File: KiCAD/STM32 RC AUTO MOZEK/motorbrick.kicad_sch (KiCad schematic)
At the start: 6 parts, among them J2 Conn_01x02_Socket, J3 Conn_01x02_Socket, J4 Conn_01x02_Socket, J5 Conn_01x02_Socket, J6 Conn_01x02_Socket, J7 Conn_01x02_Socket

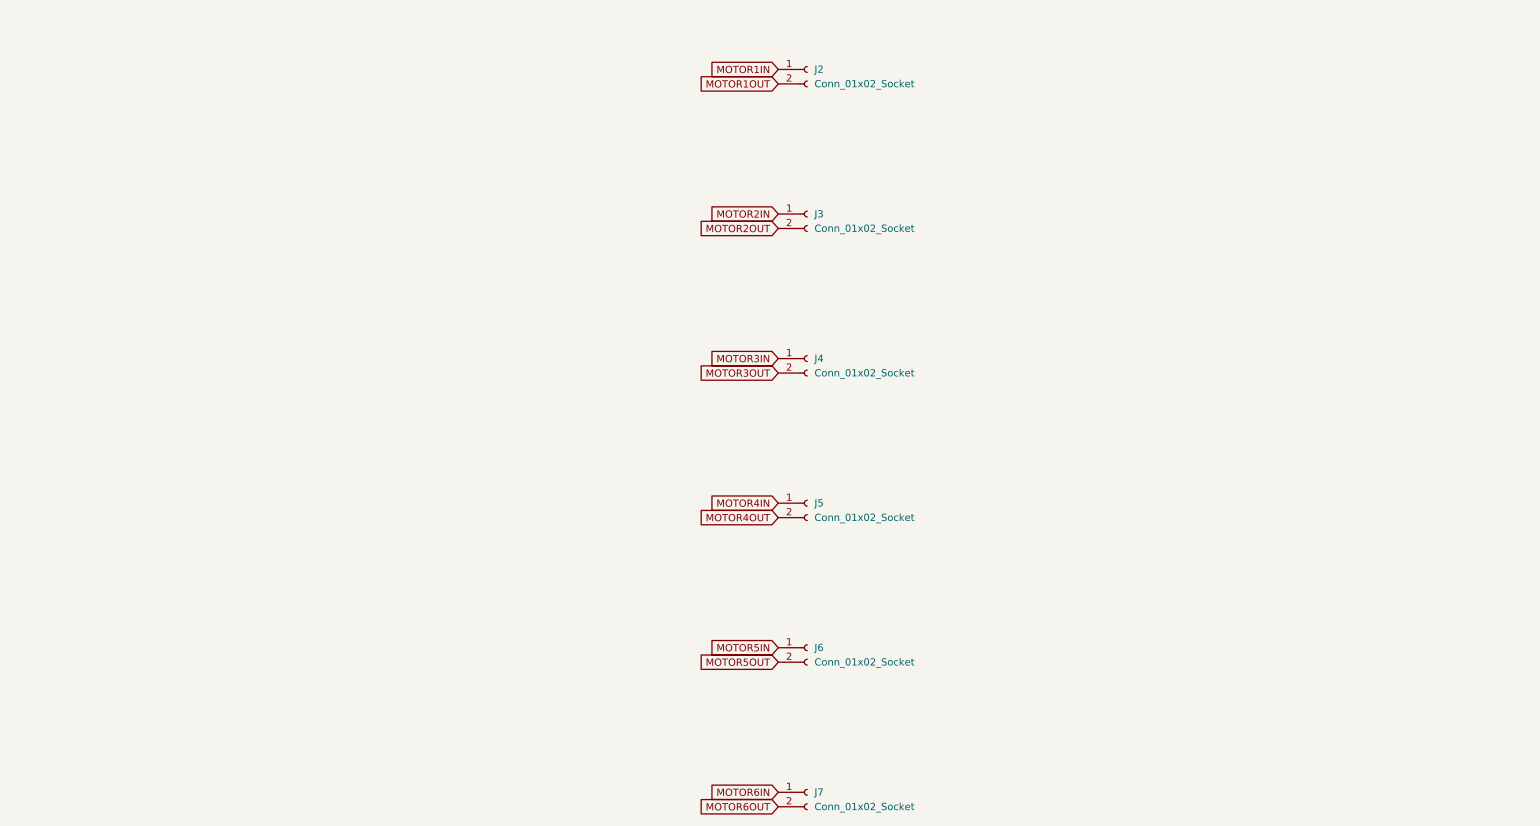
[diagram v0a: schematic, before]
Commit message: Motor power brick implementation
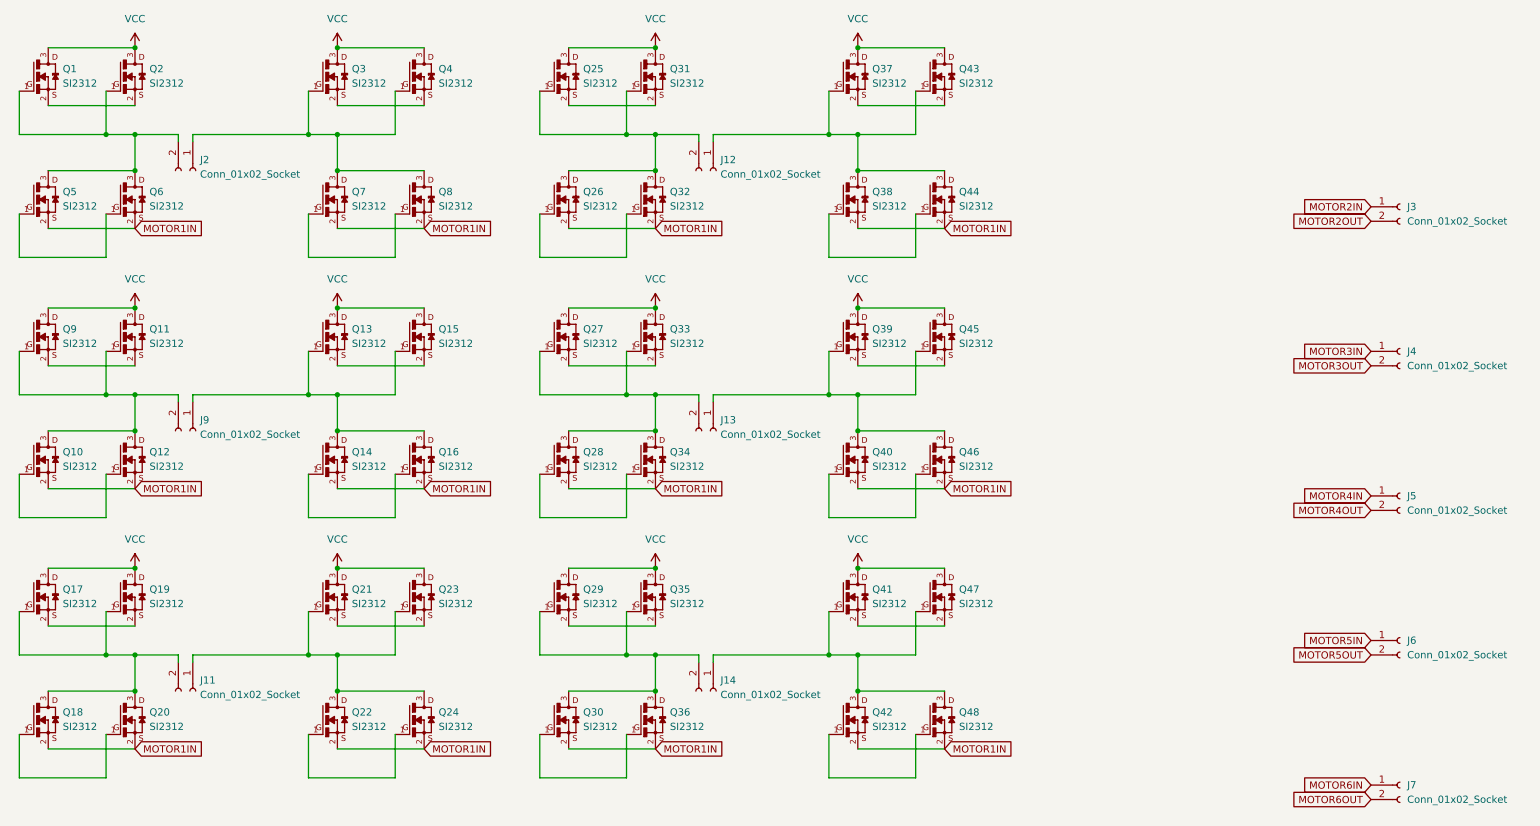
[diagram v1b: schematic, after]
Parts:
- added J11, J12, J13, J14, J9: Conn_01x02_Socket, Connector_Wire:SolderWire-2sqmm_1x02_P7.8mm_D2mm_OD3.9mm_Relief, symbol Connector:Conn_01x02_Socket
- added Q1, Q10, Q11, Q12, Q13, Q14, Q15, Q16, Q17, Q18, Q19, Q2, Q20, Q21, Q22, Q23, Q24, Q25, Q26, Q27, Q28, Q29, Q3, Q30, Q31, Q32, Q33, Q34, Q35, Q36, Q37, Q38, Q39, Q4, Q40, Q41, Q42, Q43, Q44, Q45, Q46, Q47, Q48, Q5, Q6, Q7, Q8, Q9: SI2312, SI2312:SOT23, symbol SI2312:SI2312
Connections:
- net MOTOR1IN: now also Q10.2, Q12.2, Q14.2, Q16.2, Q18.2, Q20.2, Q22.2, Q24.2, Q26.2, Q28.2, Q30.2, Q32.2, Q34.2, Q36.2, Q38.2, Q40.2, Q42.2, Q44.2, Q46.2, Q48.2, Q5.2, Q6.2, Q7.2, Q8.2; no longer J2.1 (Pin_1)
- net MOTOR1OUT: no longer names the net of J2.2 (Pin_2)
- net MOTOR1OUT: now also Q1.1, Q2.1, Q5.3, Q6.3
- new net: Q10.1, Q12.1
- new net: J9.2 (Pin_2), Q10.3, Q11.1, Q12.3, Q9.1
- new net: J11.1 (Pin_1), Q21.1, Q22.3, Q23.1, Q24.3
- new net: Q21.2, Q23.2
- new net: Q11.2, Q9.2
- new net: Q22.1, Q24.1
- new net: Q5.1, Q6.1
- new net: J2.1 (Pin_1), Q3.1, Q4.1, Q7.3, Q8.3
- new net: Q3.2, Q4.2
- new net: Q14.1, Q16.1
- new net: J9.1 (Pin_1), Q13.1, Q14.3, Q15.1, Q16.3
- new net: Q40.1, Q46.1
- new net: J13.1 (Pin_1), Q39.1, Q40.3, Q45.1, Q46.3
- new net: Q42.1, Q48.1
- new net: J14.1 (Pin_1), Q41.1, Q42.3, Q47.1, Q48.3
- new net: Q1.2, Q2.2
- new net: Q18.1, Q20.1
- new net: J11.2 (Pin_2), Q17.1, Q18.3, Q19.1, Q20.3
- new net: J12.1 (Pin_1), Q37.1, Q38.3, Q43.1, Q44.3
- new net: Q37.2, Q43.2
- new net: Q30.1, Q36.1
- new net: J14.2 (Pin_2), Q29.1, Q30.3, Q35.1, Q36.3
- new net: Q39.2, Q45.2
- new net: Q38.1, Q44.1
- new net: Q17.2, Q19.2
- new net: J13.2 (Pin_2), Q27.1, Q28.3, Q33.1, Q34.3
- new net: Q27.2, Q33.2
- new net: Q29.2, Q35.2
- new net: Q28.1, Q34.1
- new net: Q13.2, Q15.2
- new net: Q41.2, Q47.2
- new net: J12.2 (Pin_2), Q25.1, Q26.3, Q31.1, Q32.3
- new net: Q25.2, Q31.2
- new net: Q26.1, Q32.1
- new net: Q7.1, Q8.1
- new net VCC: Q1.3, Q11.3, Q13.3, Q15.3, Q17.3, Q19.3, Q2.3, Q21.3, Q23.3, Q25.3, Q27.3, Q29.3, Q3.3, Q31.3, Q33.3, Q35.3, Q37.3, Q39.3, Q4.3, Q41.3, Q43.3, Q45.3, Q47.3, Q9.3
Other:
- moved on the sheet: J2, J3, J4, J5, J6, J7

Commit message: Multi ADD
Completed work version of code and did more work on schematic
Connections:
- net MOTOR1IN: no longer Q10.2, Q12.2, Q14.2, Q16.2, Q18.2, Q20.2, Q22.2, Q24.2, Q26.2, Q28.2, Q30.2, Q32.2, Q34.2, Q36.2, Q38.2, Q40.2, Q42.2, Q44.2, Q46.2, Q48.2
- net MOTOR2IN: now also Q10.2, Q12.2, Q14.2, Q16.2
- net MOTOR3IN: now also Q18.2, Q20.2, Q22.2, Q24.2
- net MOTOR4IN: now also Q26.2, Q32.2, Q38.2, Q44.2
- net MOTOR5IN: now also Q28.2, Q34.2, Q40.2, Q46.2
- net MOTOR6IN: now also Q30.2, Q36.2, Q42.2, Q48.2
- net MOTOR2b: now reaches Q10.1, Q12.1
- net MOTOR2b: now also Q13.1, Q15.1
- net at J9.2 (Pin_2), Q10.3, Q12.3: now also Q11.2, Q9.2; no longer Q11.1, Q9.1
- net MOTOR3b: now reaches J11.1 (Pin_1), Q22.3, Q24.3
- net MOTOR3b: now also Q18.1, Q20.1, Q21.2, Q23.2; no longer Q21.1, Q23.1
- net MOTOR3a: now reaches Q22.1, Q24.1
- net MOTOR3a: now also Q17.1, Q19.1
- net MOTOR1b: now reaches Q5.1, Q6.1
- net MOTOR1b: now also Q3.1, Q4.1
- net at J2.2 (Pin_2), Q5.3, Q6.3: now also Q1.2, Q2.2; no longer Q1.1, Q2.1
- net at J2.1 (Pin_1), Q7.3, Q8.3: now also Q3.2, Q4.2; no longer Q3.1, Q4.1
- net MOTOR2a: now reaches Q14.1, Q16.1
- net MOTOR2a: now also Q11.1, Q9.1
- net at J9.1 (Pin_1), Q14.3, Q16.3: now also Q13.2, Q15.2; no longer Q13.1, Q15.1
- net MOTOR5a: now reaches Q40.1, Q46.1
- net MOTOR5a: now also Q27.1, Q33.1
- net at J13.1 (Pin_1), Q40.3, Q46.3: now also Q39.2, Q45.2; no longer Q39.1, Q45.1
- net MOTOR6a: now reaches Q42.1, Q48.1
- net MOTOR6a: now also Q29.1, Q35.1
- net at J14.1 (Pin_1), Q42.3, Q48.3: now also Q41.2, Q47.2; no longer Q41.1, Q47.1
- net at J11.2 (Pin_2), Q18.3, Q20.3: now also Q17.2, Q19.2; no longer Q17.1, Q19.1
- net at J12.1 (Pin_1), Q38.3, Q44.3: now also Q37.2, Q43.2; no longer Q37.1, Q43.1
- net MOTOR6b: now reaches Q30.1, Q36.1
- net MOTOR6b: now also Q41.1, Q47.1
- net at J14.2 (Pin_2), Q30.3, Q36.3: now also Q29.2, Q35.2; no longer Q29.1, Q35.1
- net MOTOR4a: now reaches Q38.1, Q44.1
- net MOTOR4a: now also Q25.1, Q31.1
- net at J13.2 (Pin_2), Q28.3, Q34.3: now also Q27.2, Q33.2; no longer Q27.1, Q33.1
- net MOTOR5b: now reaches Q28.1, Q34.1
- net MOTOR5b: now also Q39.1, Q45.1
- net at J12.2 (Pin_2), Q26.3, Q32.3: now also Q25.2, Q31.2; no longer Q25.1, Q31.1
- net MOTOR4b: now reaches Q26.1, Q32.1
- net MOTOR4b: now also Q37.1, Q43.1
- net MOTOR1a: now reaches Q7.1, Q8.1
- net MOTOR1a: now also Q1.1, Q2.1
- new net: Q21.1, Q23.1

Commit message: .
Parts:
- removed J3, J4, J5, J6, J7: Conn_01x02_Socket, Connector_Wire:SolderWire-2sqmm_1x02_P7.8mm_D2mm_OD3.9mm_Relief, symbol Connector:Conn_01x02_Socket

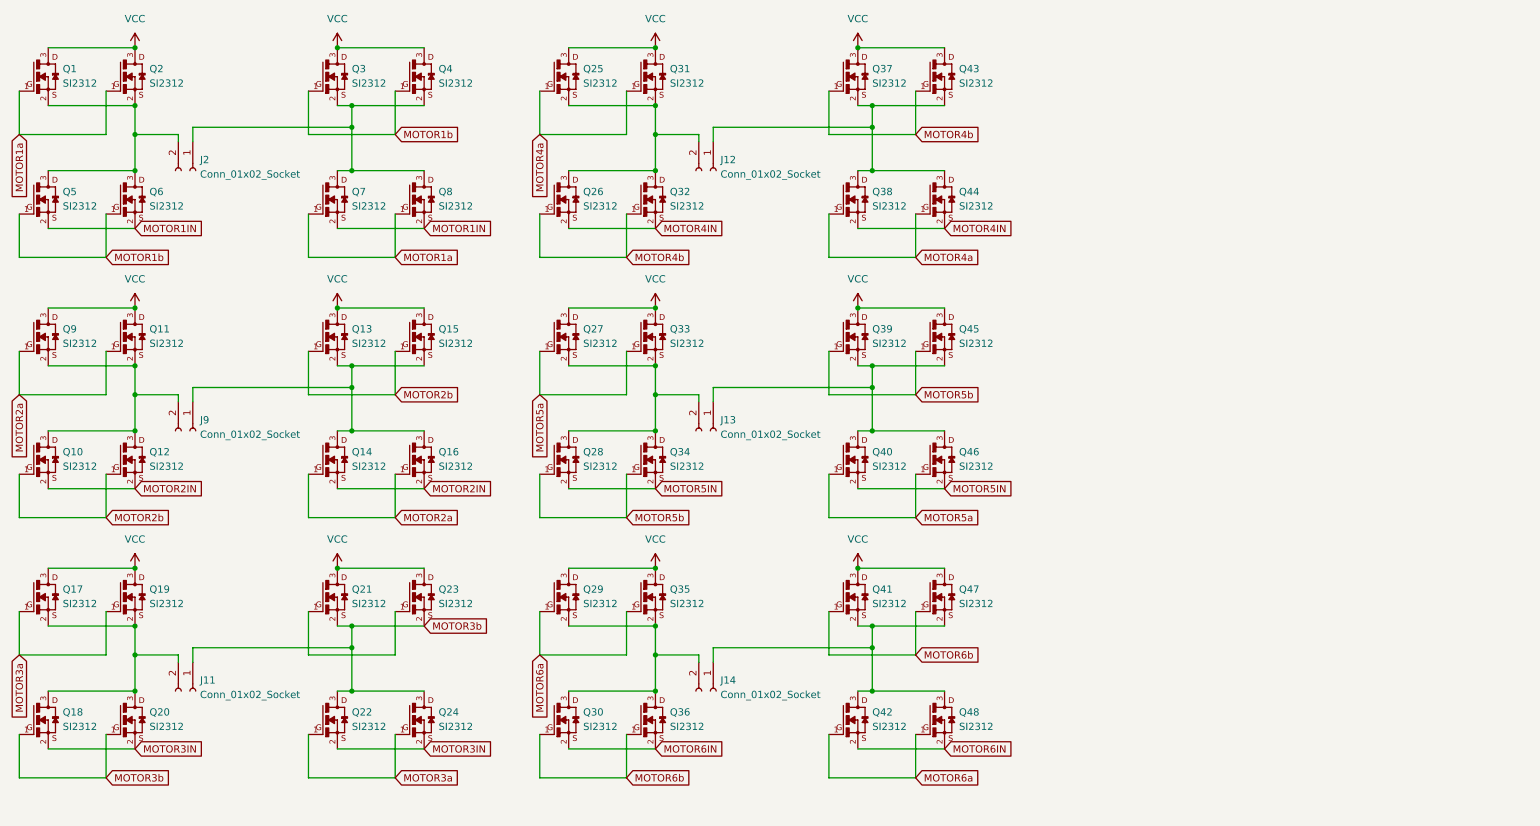
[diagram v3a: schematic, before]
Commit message: adding completation on schematic, working on board
need to add SWD Debug as input for programing
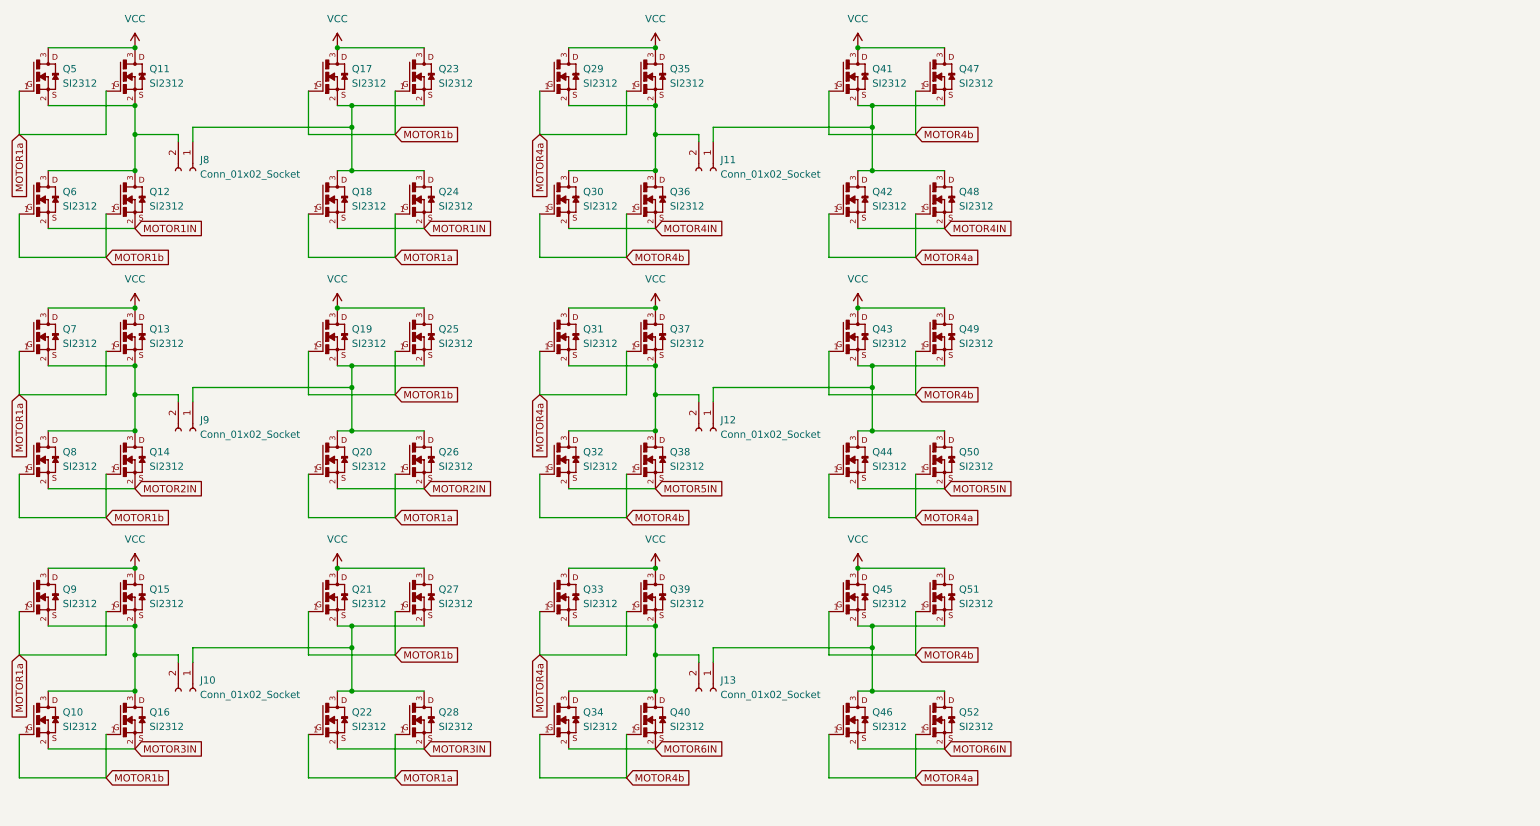
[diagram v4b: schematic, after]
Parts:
- J10: renamed from J11; footprint Connector_Wire:SolderWire-2sqmm_1x02_P7.8mm_D2mm_OD3.9mm_Relief -> Connector_Wire:SolderWire-2sqmm_1x02_P7.8mm_D2mm_OD3.9mm
- J11: renamed from J12; footprint Connector_Wire:SolderWire-2sqmm_1x02_P7.8mm_D2mm_OD3.9mm_Relief -> Connector_Wire:SolderWire-2sqmm_1x02_P7.8mm_D2mm_OD3.9mm
- J12: renamed from J13; footprint Connector_Wire:SolderWire-2sqmm_1x02_P7.8mm_D2mm_OD3.9mm_Relief -> Connector_Wire:SolderWire-2sqmm_1x02_P7.8mm_D2mm_OD3.9mm
- J13: renamed from J14; footprint Connector_Wire:SolderWire-2sqmm_1x02_P7.8mm_D2mm_OD3.9mm_Relief -> Connector_Wire:SolderWire-2sqmm_1x02_P7.8mm_D2mm_OD3.9mm
- J8: renamed from J2; footprint Connector_Wire:SolderWire-2sqmm_1x02_P7.8mm_D2mm_OD3.9mm_Relief -> Connector_Wire:SolderWire-2sqmm_1x02_P7.8mm_D2mm_OD3.9mm
- J9: footprint Connector_Wire:SolderWire-2sqmm_1x02_P7.8mm_D2mm_OD3.9mm_Relief -> Connector_Wire:SolderWire-2sqmm_1x02_P7.8mm_D2mm_OD3.9mm
- renumbered Q18 to Q10, Q2 to Q11, Q6 to Q12, Q11 to Q13, Q12 to Q14, Q19 to Q15, Q20 to Q16, Q3 to Q17, Q7 to Q18, Q13 to Q19, Q14 to Q20, Q4 to Q23, Q8 to Q24, Q15 to Q25, Q16 to Q26, Q23 to Q27, Q24 to Q28, Q25 to Q29, Q26 to Q30, Q27 to Q31, Q28 to Q32, Q29 to Q33, Q30 to Q34, Q31 to Q35, Q32 to Q36, Q33 to Q37, Q34 to Q38, Q35 to Q39, Q36 to Q40, Q37 to Q41, Q38 to Q42, Q39 to Q43, Q40 to Q44, Q41 to Q45, Q42 to Q46, Q43 to Q47, Q44 to Q48, Q45 to Q49, Q1 to Q5, Q46 to Q50, Q47 to Q51, Q48 to Q52, Q5 to Q6, Q9 to Q7, Q10 to Q8, Q17 to Q9
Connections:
- net MOTOR2a is gone; now on net MOTOR1a: Q13.1, Q20.1, Q26.1, Q7.1
- net MOTOR2b is gone; now on net MOTOR1b: Q14.1, Q19.1, Q25.1, Q8.1
- net MOTOR3a is gone; now on net MOTOR1a: Q15.1, Q22.1, Q28.1, Q9.1
- net MOTOR5a is gone; now on net MOTOR4a: Q31.1, Q37.1, Q44.1, Q50.1
- net MOTOR5b is gone; now on net MOTOR4b: Q32.1, Q38.1, Q43.1, Q49.1
- net MOTOR6a is gone; now on net MOTOR4a: Q33.1, Q39.1, Q46.1, Q52.1
- net MOTOR6b is gone; now on net MOTOR4b: Q34.1, Q40.1, Q45.1, Q51.1
- net MOTOR1b: now also Q10.1, Q16.1, Q21.1, Q27.1
- net MOTOR3b: no longer names the net of J10.1 (Pin_1), Q21.2, Q22.3, Q27.2, Q28.3
- net MOTOR3b: no longer Q10.1, Q16.1

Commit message: .
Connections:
- net MOTOR4a renamed MOTOR2a
- net MOTOR4b renamed MOTOR2b
